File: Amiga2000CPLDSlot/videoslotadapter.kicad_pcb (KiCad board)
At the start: 2 copper layers, 152 x 57.6 mm, 13 parts, among them J1 Raspberry_Pi_2_3, J2 JTAG, U1 XC9572VQ44

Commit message: Amiga2000CPLDSlot v1.1
Made the following changes after some Discord chats:

* Added optional buttons 2 & 3
* Added an arrow to point to the rear of the Amiga
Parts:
- added JButton3: Conn_01x02, Connector_PinHeader_2.54mm:PinHeader_1x02_P2.54mm_Horizontal, F.Cu at (116.5, 87.1)
- added JButton4: Conn_01x02, Connector_PinHeader_2.54mm:PinHeader_1x02_P2.54mm_Horizontal, F.Cu at (199.1, 84.7)
- added JButton5: Conn_01x02, Connector_PinHeader_2.54mm:PinHeader_1x02_P2.54mm_Horizontal, F.Cu at (116.5, 79.1)
- added JButton6: Conn_01x02, Connector_PinHeader_2.54mm:PinHeader_1x02_P2.54mm_Horizontal, F.Cu at (199.1, 76.7)
- moved JButton1 0.13 mm to (199.1, 68.7)
- moved JButton2 0.07 mm to (116.5, 71.1)
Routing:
- net /GPIO19: track 0.00 -> 108.7 mm, vias 0 -> 1
- net /GPIO26: track 0.00 -> 96.0 mm, vias 0 -> 1
- net /GPIO16: track 97.2 -> 98.3 mm
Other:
- board text added: "Amiga video slot RGBtoHDMI CPLD v1.1 (C) 2021 LinuxJedi Based on work by IanSB, hoglet67 and Bloodmosher https://github.com/LinuxJedi/AmigaRGBtoHDMI"
- board text added: "Button 1"
- board text added: "Button 2"
- board text added: "Button 3"
- board text added: "TOWARDS REAR OF AMIGA"
- board text removed: "Amiga video slot RGBtoHDMI CPLD v1 (C) 2021 LinuxJedi Based on work by IanSB, hoglet67 and Bloodmosher https://github.com/LinuxJedi/AmigaRGBtoHDMI"
- board text removed: "Button"

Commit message: Make things clearer
* After feedback on the GPIO JTAG programming section I've made this
  clearer
* Added silk to the A2000 CPLD slot to mark the wrong way around
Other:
- board text added: "IF YOU CAN READ THIS AND I'M IN YOUR AMIGA I'M THE WRONG WAY AROUND!"

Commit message: Final tested release of Amiga 2000 CPLD edition
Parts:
- removed J2: JTAG, Connector_PinHeader_2.54mm:PinHeader_1x06_P2.54mm_Vertical
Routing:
- net /GPIO20: track 110.8 -> 44.9 mm, vias 1 -> 0
- net /CLKEN: track 83.4 -> 26.1 mm, vias 2 -> 0
- net /GPIO0: track 88.7 -> 32.4 mm
- net /GPIO24: track 56.9 -> 18.8 mm, vias 1 -> 0
- net +3V3: track 108.7 -> 98.0 mm, vias 7 -> 6
- net /GPIO26: track 96.0 -> 103.8 mm, vias 1 -> 0
- net /GPIO16: track 98.3 -> 100.4 mm
- net /GPIO19: track 108.7 -> 108.3 mm, vias 1 -> 0
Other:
- board text added: "Amiga video slot RGBtoHDMI CPLD v1.2 (C) 2021 LinuxJedi Based on work by IanSB, hoglet67 and Bloodmosher https://github.com/LinuxJedi/AmigaRGBtoHDMI"
- board text added: "Development sponsored by: Richard Lake Charles Underwood"
- board text added: "IF YOU CAN READ THIS, YOUR PI IS UPSIDE DOWN!"
- board text removed: "Amiga video slot RGBtoHDMI CPLD v1.1 (C) 2021 LinuxJedi Based on work by IanSB, hoglet67 and Bloodmosher https://github.com/LinuxJedi/AmigaRGBtoHDMI"

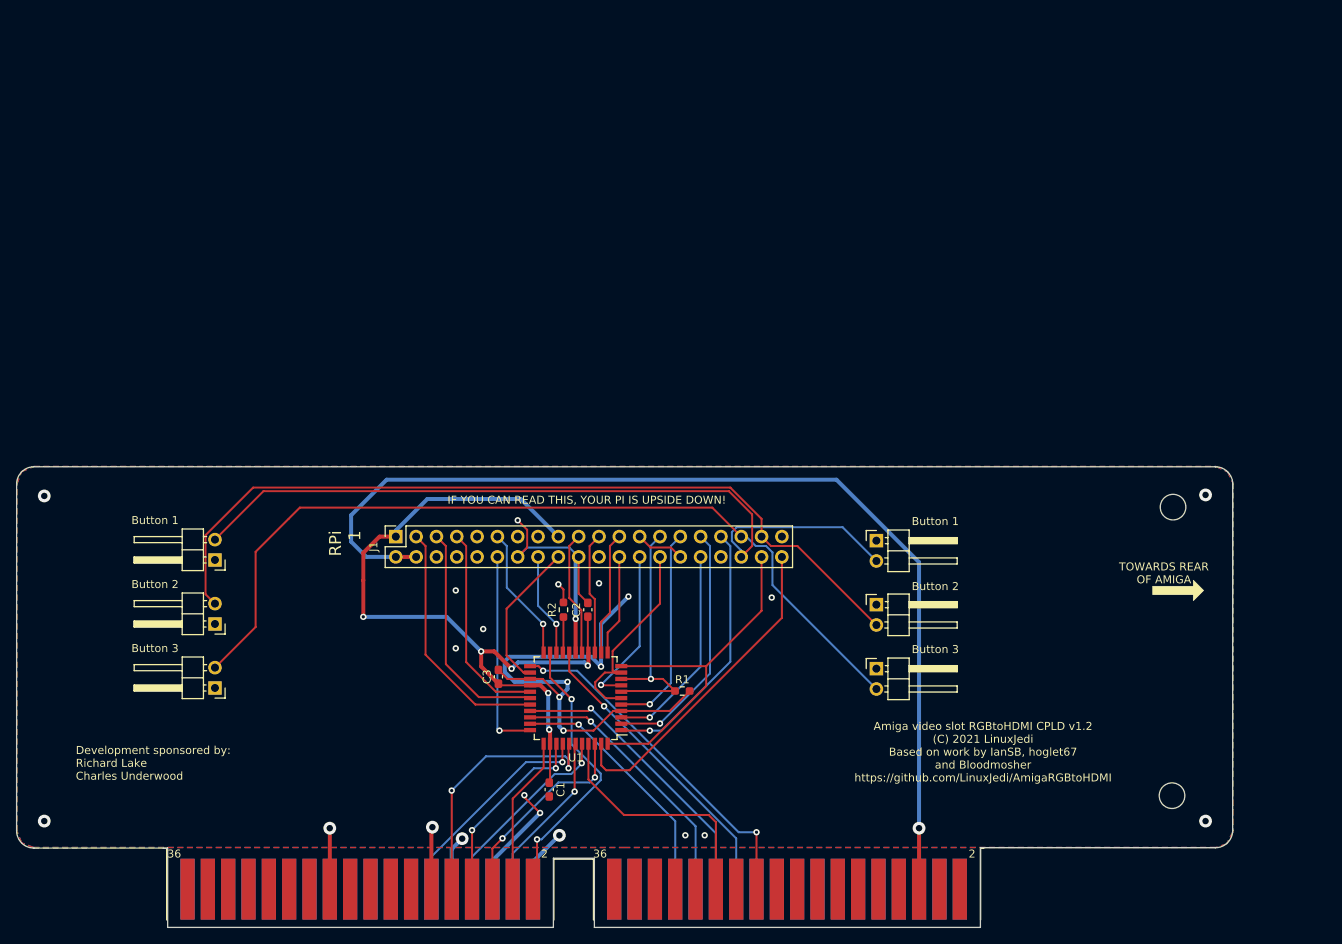
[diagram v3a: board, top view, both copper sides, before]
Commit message: Add Amiga 2000 CPLD v2.1
Adds the Amiga 2000 CPLD v2.1 and moves older boards to legacy.
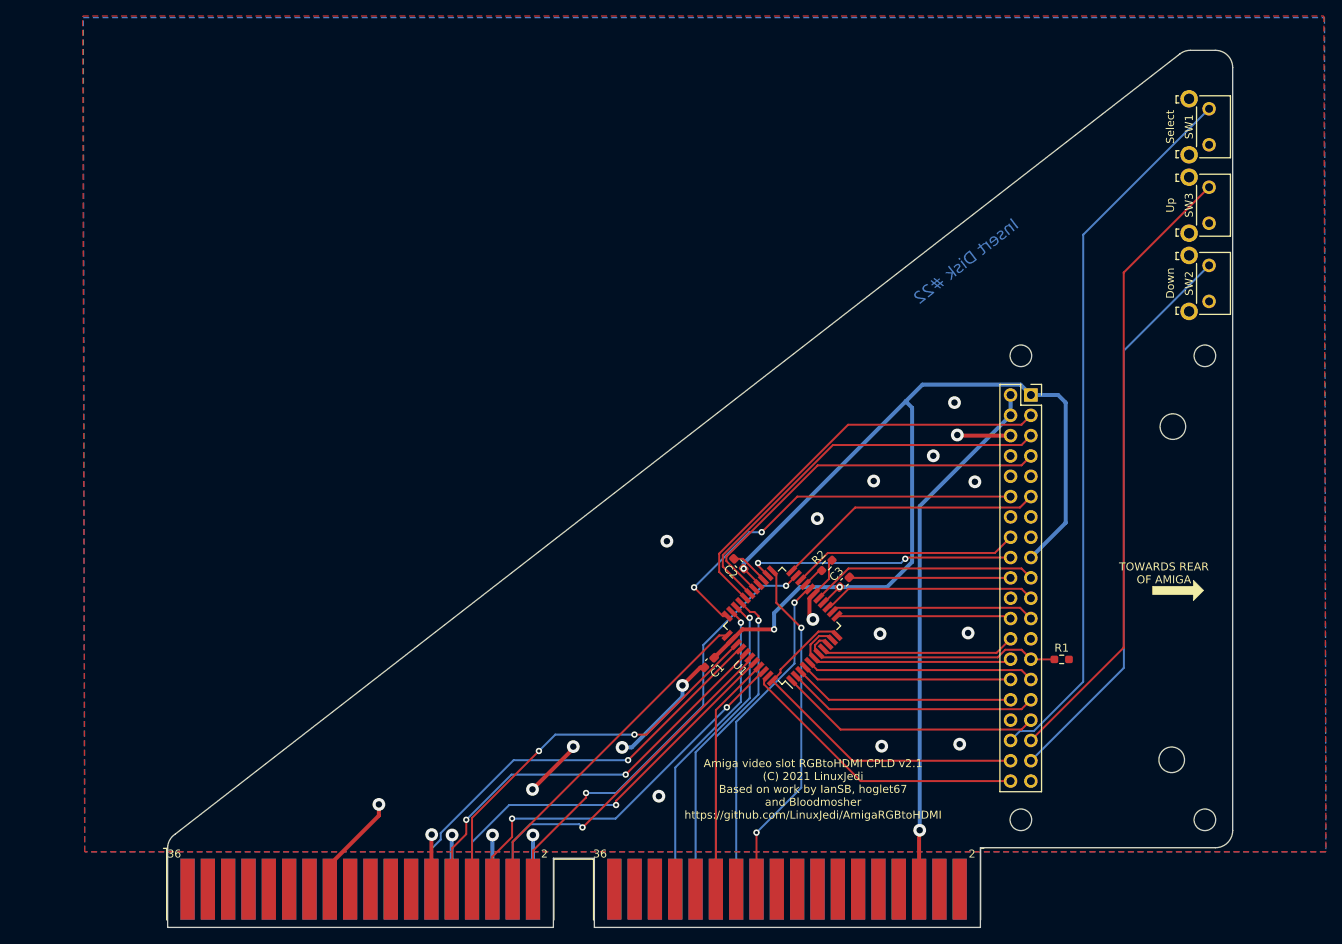
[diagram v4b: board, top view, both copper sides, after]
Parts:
- removed JButton1, JButton2, JButton3, JButton4, JButton5, JButton6: Conn_01x02, Connector_PinHeader_2.54mm:PinHeader_1x02_P2.54mm_Horizontal
- added H3: MountingHole, MountingHole:MountingHole_2.7mm_M2.5, F.Cu at (217.2, 103.6)
- added H4: MountingHole, MountingHole:MountingHole_2.7mm_M2.5, F.Cu at (217.2, 45.6)
- added H5: MountingHole, MountingHole:MountingHole_2.7mm_M2.5, F.Cu at (240.2, 103.6)
- added H6: MountingHole, MountingHole:MountingHole_2.7mm_M2.5, F.Cu at (240.2, 45.6)
- added SW1: Select, Button_Switch_THT:SW_Tactile_SKHH_Angled, F.Cu at (240.7, 14.7)
- added SW2: Down, Button_Switch_THT:SW_Tactile_SKHH_Angled, F.Cu at (240.7, 34.3)
- added SW3: Up, Button_Switch_THT:SW_Tactile_SKHH_Angled, F.Cu at (240.7, 24.5)
- moved J1 81.3 mm to (218.4, 50.5), turned to 0 degrees
- moved R1 47.6 mm to (222.3, 83.5)
- moved C3 44.8 mm to (195.2, 73.9), turned to 45 degrees
- moved R2 33.4 mm to (192.9, 71.8), turned to 45 degrees
- moved U1 27.3 mm to (187.3, 79.3), turned to 135 degrees
- moved C1 25.5 mm to (178.2, 84.0), turned to -135 degrees
- moved C2 19.7 mm to (181.9, 71.6), turned to 135 degrees
- moved H1 10.1 mm to (236.2, 54.5)
- moved H2 4.48 mm to (236.1, 96.1)
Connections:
- JVideoSlot1 pad 1: Net-(JVideoSlot1-Pad1) -> unconnected-(JVideoSlot1-Reserved)_1
- JVideoSlot1 pad 10: Net-(JVideoSlot1-Pad10) -> unconnected-(JVideoSlot1-+12_VDC_(8A))
- JVideoSlot1 pad 11: Net-(JVideoSlot1-Pad11) -> unconnected-(JVideoSlot1-Analog_Green)
- JVideoSlot1 pad 12: Net-(JVideoSlot1-Pad12) -> unconnected-(JVideoSlot1-Video_Ground)_1
- JVideoSlot1 pad 13: Net-(JVideoSlot1-Pad13) -> unconnected-(JVideoSlot1-Video_Ground)_2
- JVideoSlot1 pad 14: Net-(JVideoSlot1-Pad14) -> unconnected-(JVideoSlot1-/CSYNC)
- JVideoSlot1 pad 15: Net-(JVideoSlot1-Pad15) -> unconnected-(JVideoSlot1-Analog_Blue)
- JVideoSlot1 pad 16: Net-(JVideoSlot1-Pad16) -> unconnected-(JVideoSlot1-/XCLKEN)
- JVideoSlot1 pad 17: Net-(JVideoSlot1-Pad17) -> unconnected-(JVideoSlot1-Video_Ground)_3
- JVideoSlot1 pad 18: Net-(JVideoSlot1-Pad18) -> unconnected-(JVideoSlot1-Burst)
- JVideoSlot1 pad 19: Net-(JVideoSlot1-Pad19) -> unconnected-(JVideoSlot1-/C4_Clock)
- JVideoSlot1 pad 2: Net-(JVideoSlot1-Pad2) -> unconnected-(JVideoSlot1-Reserved)_2
- JVideoSlot1 pad 20: Net-(JVideoSlot1-Pad20) -> unconnected-(JVideoSlot1-Video_Ground)_4
- JVideoSlot1 pad 21: Net-(JVideoSlot1-Pad21) -> unconnected-(JVideoSlot1-Video_Ground)_5
- JVideoSlot1 pad 24: Net-(JVideoSlot1-Pad24) -> unconnected-(JVideoSlot1-Video_Ground)_6
- JVideoSlot1 pad 28: Net-(JVideoSlot1-Pad28) -> unconnected-(JVideoSlot1-COMP_SYNC(Analog))
- JVideoSlot1 pad 3: Net-(JVideoSlot1-Pad3) -> unconnected-(JVideoSlot1-Audio_Out_Left)
- JVideoSlot1 pad 30: Net-(JVideoSlot1-Pad30) -> unconnected-(JVideoSlot1-/PIXELSW(47-Ohm))
- JVideoSlot1 pad 31: Net-(JVideoSlot1-Pad31) -> unconnected-(JVideoSlot1--5_VDC_(0.3A))
- JVideoSlot1 pad 32: Net-(JVideoSlot1-Pad32) -> unconnected-(JVideoSlot1-Video_Ground)
- JVideoSlot1 pad 33: Net-(JVideoSlot1-Pad33) -> unconnected-(JVideoSlot1-XCLK)
- JVideoSlot1 pad 34: Net-(JVideoSlot1-Pad34) -> unconnected-(JVideoSlot1-/C1_Clock)
- JVideoSlot1 pad 35: Net-(JVideoSlot1-Pad35) -> unconnected-(JVideoSlot1-Reserved)_3
- JVideoSlot1 pad 36: Net-(JVideoSlot1-Pad36) -> unconnected-(JVideoSlot1-Reserved)_4
- JVideoSlot1 pad 4: Net-(JVideoSlot1-Pad4) -> unconnected-(JVideoSlot1-Audio_Out_Right)
- JVideoSlot1 pad 49: Net-(JVideoSlot1-Pad49) -> unconnected-(JVideoSlot1-Composite_Video)
- JVideoSlot1 pad 5: Net-(JVideoSlot1-Pad5) -> unconnected-(JVideoSlot1-Reserved)
- JVideoSlot1 pad 50: Net-(JVideoSlot1-Pad50) -> unconnected-(JVideoSlot1-TBASE)
- JVideoSlot1 pad 51: Net-(JVideoSlot1-Pad51) -> unconnected-(JVideoSlot1-CDAC_Clock)
- JVideoSlot1 pad 52: Net-(JVideoSlot1-Pad52) -> unconnected-(JVideoSlot1-POUT)
- JVideoSlot1 pad 53: Net-(JVideoSlot1-Pad53) -> unconnected-(JVideoSlot1-/C3_Clock)
- JVideoSlot1 pad 54: Net-(JVideoSlot1-Pad54) -> unconnected-(JVideoSlot1-BUSY)
- JVideoSlot1 pad 55: Net-(JVideoSlot1-Pad55) -> unconnected-(JVideoSlot1-/LPEN)
- JVideoSlot1 pad 56: Net-(JVideoSlot1-Pad56) -> unconnected-(JVideoSlot1-/ACK)
- JVideoSlot1 pad 57: Net-(JVideoSlot1-Pad57) -> unconnected-(JVideoSlot1-SEL)
- JVideoSlot1 pad 59: Net-(JVideoSlot1-Pad59) -> unconnected-(JVideoSlot1-PD0)
- JVideoSlot1 pad 60: Net-(JVideoSlot1-Pad60) -> unconnected-(JVideoSlot1-PD1)
- JVideoSlot1 pad 61: Net-(JVideoSlot1-Pad61) -> unconnected-(JVideoSlot1-PD2)
- JVideoSlot1 pad 62: Net-(JVideoSlot1-Pad62) -> unconnected-(JVideoSlot1-PD3)
- JVideoSlot1 pad 63: Net-(JVideoSlot1-Pad63) -> unconnected-(JVideoSlot1-PD4)
- JVideoSlot1 pad 64: Net-(JVideoSlot1-Pad64) -> unconnected-(JVideoSlot1-PD5)
- JVideoSlot1 pad 65: Net-(JVideoSlot1-Pad65) -> unconnected-(JVideoSlot1-PD6)
- JVideoSlot1 pad 66: Net-(JVideoSlot1-Pad66) -> unconnected-(JVideoSlot1-PD7)
- JVideoSlot1 pad 67: Net-(JVideoSlot1-Pad67) -> unconnected-(JVideoSlot1-/LED)
- JVideoSlot1 pad 68: Net-(JVideoSlot1-Pad68) -> unconnected-(JVideoSlot1-Ground)
- JVideoSlot1 pad 69: Net-(JVideoSlot1-Pad69) -> unconnected-(JVideoSlot1-Raw_Audio_Left)
- JVideoSlot1 pad 7: Net-(JVideoSlot1-Pad7) -> unconnected-(JVideoSlot1-Analog_Red)
- JVideoSlot1 pad 70: Net-(JVideoSlot1-Pad70) -> unconnected-(JVideoSlot1-Audio_Ground)_1
- JVideoSlot1 pad 71: Net-(JVideoSlot1-Pad71) -> unconnected-(JVideoSlot1-Raw_Audio_Right)
- JVideoSlot1 pad 72: Net-(JVideoSlot1-Pad72) -> unconnected-(JVideoSlot1-Audio_Ground)
- JVideoSlot1 pad 8: Net-(JVideoSlot1-Pad8) -> unconnected-(JVideoSlot1-+5_VDC_(2A))
- JVideoSlot1 pad 9: Net-(JVideoSlot1-Pad9) -> unconnected-(JVideoSlot1-Video_Green)
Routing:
- net VCC: track 130.2 -> 66.5 mm
- net +3V3: track 98.0 -> 132.3 mm, vias 6 -> 3
- net /GPIO26: track 103.8 -> 71.1 mm
- net /GPIO19: track 108.3 -> 78.4 mm
- net /B2: track 27.7 -> 54.5 mm
- net /G2: track 24.2 -> 50.9 mm
- net /G1: track 25.1 -> 50.8 mm
- net /GPIO18: track 25.7 -> 49.9 mm, vias 1 -> 2
- net /R1: track 21.4 -> 45.6 mm
- net /R2: track 19.8 -> 43.4 mm
- net GND: track 152.9 -> 129.8 mm, vias 25 -> 22
- net /GPIO4: track 25.7 -> 48.8 mm
- net /G0: track 25.8 -> 48.9 mm
- net /GPIO3: track 28.7 -> 50.9 mm
- net /GPIO2: track 30.9 -> 53.0 mm
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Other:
- board size 152 x 57.6 mm -> 133.1 x 109.6 mm
- net class Default removed
- board text added: "Amiga video slot RGBtoHDMI CPLD v2.1 (C) 2021 LinuxJedi Based on work by IanSB, hoglet67 and Bloodmosher https://github.com/LinuxJedi/AmigaRGBtoHDMI"
- board text added: "Down"
- board text added: "Insert Disk #22"
- board text added: "Select"
- board text added: "Up"
- board text removed: "Amiga video slot RGBtoHDMI CPLD v1.2 (C) 2021 LinuxJedi Based on work by IanSB, hoglet67 and Bloodmosher https://github.com/LinuxJedi/AmigaRGBtoHDMI"
- board text removed: "Button 1"
- board text removed: "Button 2"
- board text removed: "Button 3"
- board text removed: "Development sponsored by: Richard Lake Charles Underwood"
- board text removed: "IF YOU CAN READ THIS, YOUR PI IS UPSIDE DOWN!"
- board text removed: "RPi 1"

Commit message: Add Amiga 2000 RGBtoHDMI v2.2
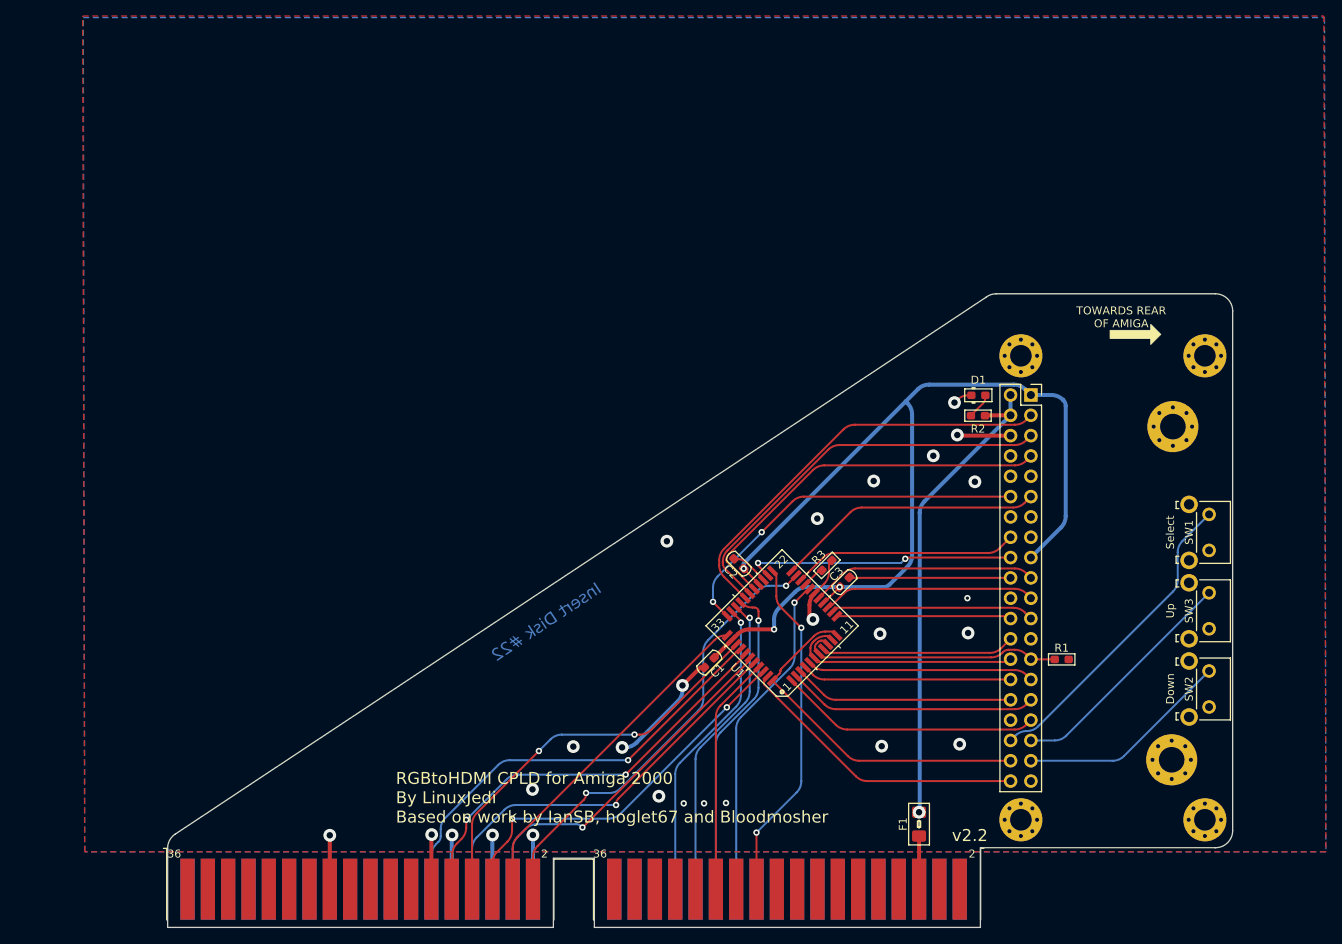
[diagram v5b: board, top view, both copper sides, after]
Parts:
- added D1: LED, Diode_SMD_Handsoldering_AKL:D_0603_1608Metric_Pad1.05x0.95mm, F.Cu at (211.9, 50.5)
- added F1: 500mA, Fuse_Handsoldering_AKL:Fuse_1206_3216Metric_Pad1.42x1.75mm_BigPads, F.Cu at (204.5, 104.1)
- added R2: R, Resistor_SMD_AKL:R_0603_1608Metric_Pad1.05x0.95mm_HandSolder, F.Cu at (211.8, 53.1)
- C1, C2, C3: footprint Capacitor_SMD:C_0603_1608Metric_Pad1.08x0.95mm_HandSolder -> Capacitor_SMD_Handsoldering_AKL:C_0603_1608Metric_Pad1.08x0.95mm
- H1: renamed from H3; footprint MountingHole:MountingHole_2.7mm_M2.5 -> MountingHole:MountingHole_2.7mm_M2.5_Pad_Via
- H2: renamed from H4; footprint MountingHole:MountingHole_2.7mm_M2.5 -> MountingHole:MountingHole_2.7mm_M2.5_Pad_Via
- H3: renamed from H5; footprint MountingHole:MountingHole_2.7mm_M2.5 -> MountingHole:MountingHole_2.7mm_M2.5_Pad_Via
- H4: renamed from H6; footprint MountingHole:MountingHole_2.7mm_M2.5 -> MountingHole:MountingHole_2.7mm_M2.5_Pad_Via
- H5: renamed from H1; footprint MountingHole:MountingHole_3.2mm_M3 -> MountingHole:MountingHole_3.2mm_M3_Pad_Via
- H6: renamed from H2; footprint MountingHole:MountingHole_3.2mm_M3 -> MountingHole:MountingHole_3.2mm_M3_Pad_Via
- R1: footprint Resistor_SMD:R_0603_1608Metric_Pad0.98x0.95mm_HandSolder -> Resistor_SMD_AKL:R_0603_1608Metric_Pad1.05x0.95mm_HandSolder
- R3: renamed from R2; footprint Resistor_SMD:R_0603_1608Metric_Pad0.98x0.95mm_HandSolder -> Resistor_SMD_AKL:R_0603_1608Metric_Pad1.05x0.95mm_HandSolder
- U1: footprint Package_QFP:TQFP-44_10x10mm_P0.8mm -> Package_QFP_AKL:TQFP-44_10x10mm_P0.8mm
- moved SW1 50.7 mm to (240.7, 65.4)
- moved SW3 50.7 mm to (240.7, 75.2)
- moved SW2 50.7 mm to (240.7, 85.0)
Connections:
- J1 pad 2: VCC -> +5V
- J1 pad 4: VCC -> +5V
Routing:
- net +5V: track 0.00 -> 60.0 mm, vias 0 -> 1
- net VCC: track 66.5 -> 6.64 mm, vias 1 -> 0
- net /GPIO16: track 90.3 -> 39.1 mm
- net /GPIO19: track 78.4 -> 29.8 mm
- net /GPIO26: track 71.1 -> 26.8 mm
- net GND: track 129.8 -> 120.2 mm, vias 22 -> 26
- net /GPIO18: track 49.9 -> 46.5 mm
- net Net-(D1-A): track 0.00 -> 3.26 mm
- net +3V3: track 132.3 -> 131.4 mm
- net /R0: track 56.8 -> 56.2 mm
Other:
- board size 133.1 x 109.6 mm -> 133.1 x 79.2 mm
- board text added: "RGBtoHDMI CPLD for Amiga 2000 By LinuxJedi Based on work by IanSB, hoglet67 and Bloodmosher"
- board text added: "v2.2"
- board text removed: "Amiga video slot RGBtoHDMI CPLD v2.1 (C) 2021 LinuxJedi Based on work by IanSB, hoglet67 and Bloodmosher https://github.com/LinuxJedi/AmigaRGBtoHDMI"
